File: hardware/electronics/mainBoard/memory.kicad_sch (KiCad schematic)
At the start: 16 parts, among them J2 MEM2067-02-180-00-A, U3 W25Q128JVP, U4 M24512-DRE

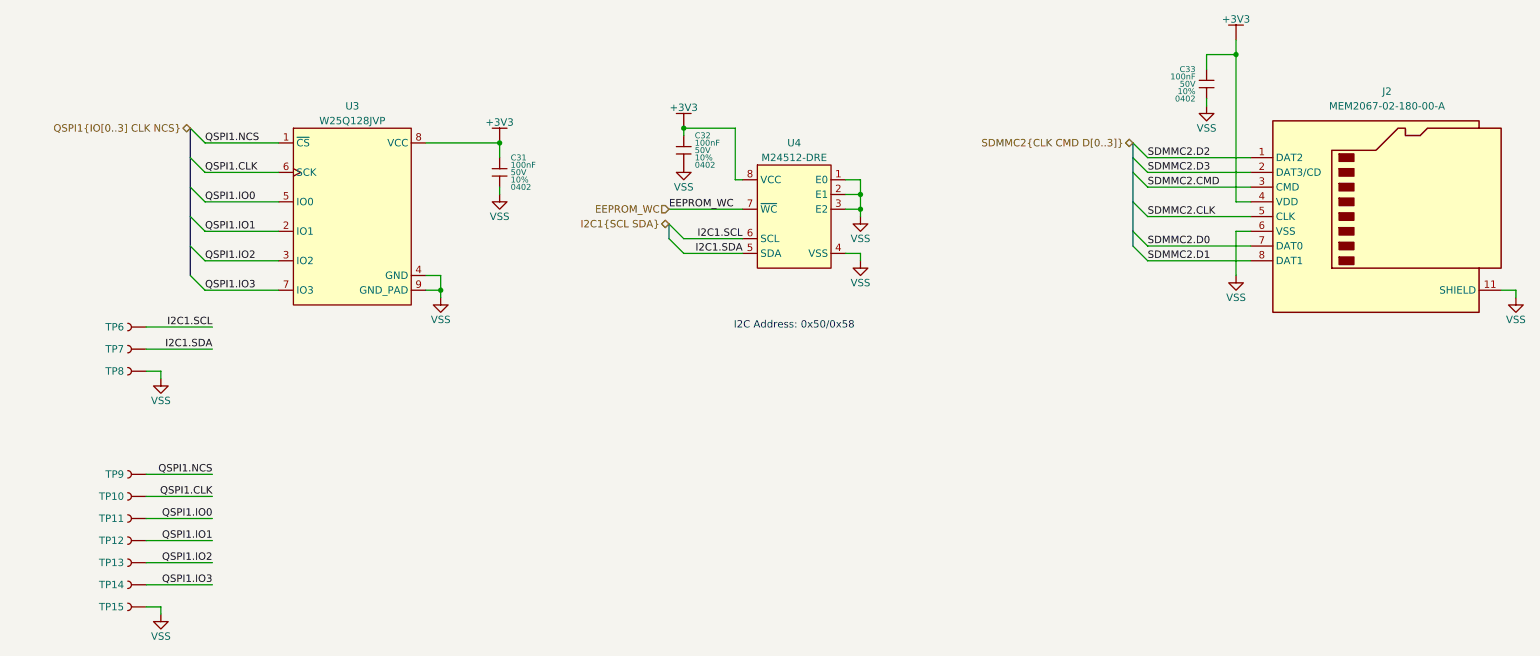
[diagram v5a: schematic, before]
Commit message: updated symbol refs
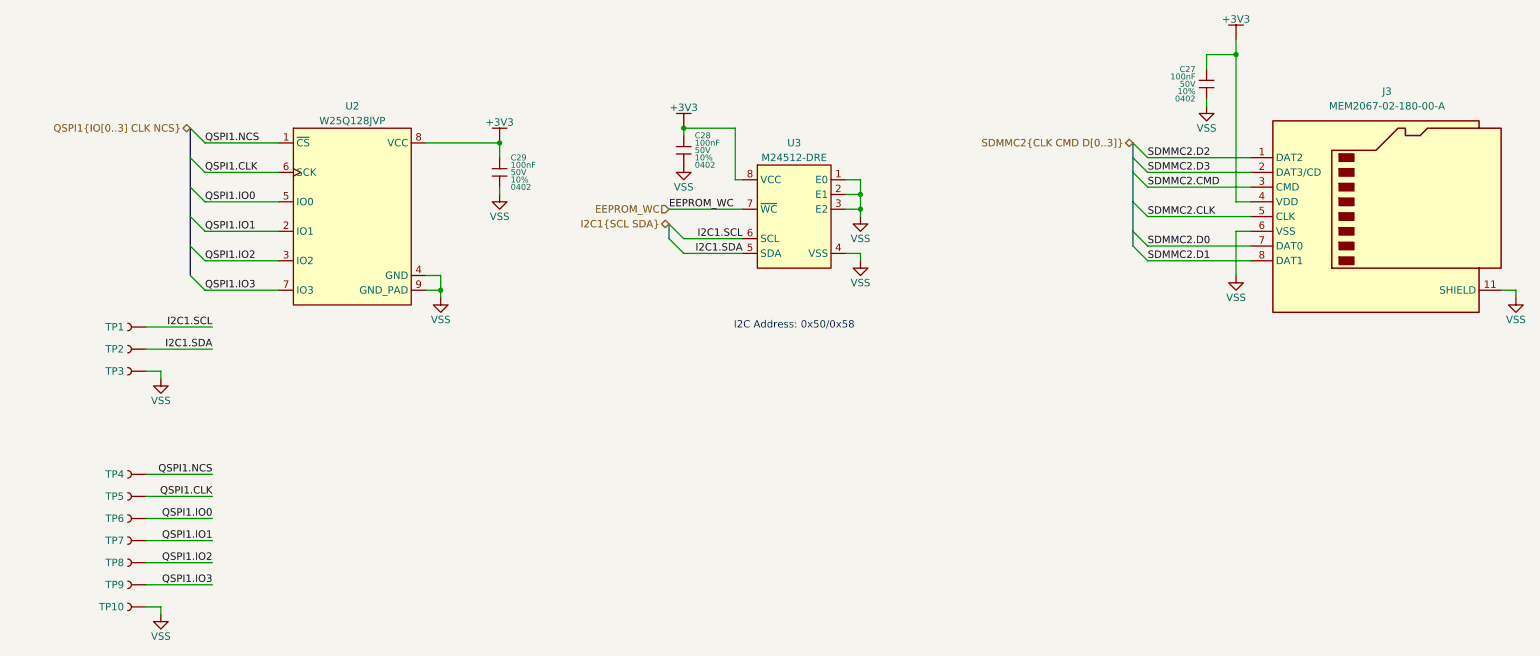
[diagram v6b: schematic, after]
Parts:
- renumbered C33 to C27, C32 to C28, C31 to C29, J2 to J3, TP6 to TP1, TP15 to TP10, TP7 to TP2, TP8 to TP3, TP9 to TP4, TP10 to TP5, TP11 to TP6, TP12 to TP7, TP13 to TP8, TP14 to TP9, U3 to U2, U4 to U3
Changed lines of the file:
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@@
 		(dnp no)
 		(fields_autoplaced yes)
-		(property "Reference" "#PWR068"
+		(property "Reference" "#PWR065"
 			(at 88.9 95.25 0)
 			(effects
@@
 			(project ""
 				(path "/be16e32f-2ccf-4272-9ec7-94d5fe7a55e0/bf9ac865-aa9a-42a1-8ada-6ec99a5fbf41"
-					(reference "#PWR068")
+					(reference "#PWR065")
 					(unit 1)
 				)
@@
 		(dnp no)
 		(fields_autoplaced yes)
-		(property "Reference" "#PWR070"
+		(property "Reference" "#PWR064"
 			(at 120.65 92.71 0)
 			(effects
@@
 			(project "mainBoard"
 				(path "/be16e32f-2ccf-4272-9ec7-94d5fe7a55e0/bf9ac865-aa9a-42a1-8ada-6ec99a5fbf41"
-					(reference "#PWR070")
+					(reference "#PWR064")
 					(unit 1)
 				)
@@
 		(dnp no)
 		(fields_autoplaced yes)
-		(property "Reference" "J2"
+		(property "Reference" "J3"
 			(at 241.935 86.36 0)
 			(effects
@@
 			(project ""
 				(path "/be16e32f-2ccf-4272-9ec7-94d5fe7a55e0/bf9ac865-aa9a-42a1-8ada-6ec99a5fbf41"
-					(reference "J2")
+					(reference "J3")
 					(unit 1)
 				)
@@
 		(on_board yes)
 		(dnp no)
-		(property "Reference" "C33"
+		(property "Reference" "C27"
 			(at 208.915 82.55 0)
 			(do_not_autoplace yes)
@@
 			(project "mainBoard"
 				(path "/be16e32f-2ccf-4272-9ec7-94d5fe7a55e0/bf9ac865-aa9a-42a1-8ada-6ec99a5fbf41"
-					(reference "C33")
+					(reference "C27")
 					(unit 1)
 				)
@@
 		(dnp no)
 		(fields_autoplaced yes)
-		(property "Reference" "TP15"
+		(property "Reference" "TP10"
 			(at 24.13 175.26 0)
 			(do_not_autoplace yes)
@@
 			(project "mainBoard"
 				(path "/be16e32f-2ccf-4272-9ec7-94d5fe7a55e0/bf9ac865-aa9a-42a1-8ada-6ec99a5fbf41"
-					(reference "TP15")
+					(reference "TP10")
 					(unit 1)
 				)
@@
 		(dnp no)
 		(fields_autoplaced yes)
-		(property "Reference" "#PWR077"
+		(property "Reference" "#PWR072"
 			(at 264.16 121.92 0)
 			(effects
@@
 			(project "mainBoard"
 				(path "/be16e32f-2ccf-4272-9ec7-94d5fe7a55e0/bf9ac865-aa9a-42a1-8ada-6ec99a5fbf41"
-					(reference "#PWR077")
+					(reference "#PWR072")
 					(unit 1)
 				)
@@
 		(dnp no)
 		(fields_autoplaced yes)
-		(property "Reference" "TP8"
+		(property "Reference" "TP3"
 			(at 24.13 134.62 0)
 			(do_not_autoplace yes)
@@
 			(project "mainBoard"
 				(path "/be16e32f-2ccf-4272-9ec7-94d5fe7a55e0/bf9ac865-aa9a-42a1-8ada-6ec99a5fbf41"
-					(reference "TP8")
+					(reference "TP3")
 					(unit 1)
 				)
@@
 		(dnp no)
 		(fields_autoplaced yes)
-		(property "Reference" "TP7"
+		(property "Reference" "TP2"
 			(at 24.13 130.81 0)
 			(do_not_autoplace yes)
@@
 			(project "mainBoard"
 				(path "/be16e32f-2ccf-4272-9ec7-94d5fe7a55e0/bf9ac865-aa9a-42a1-8ada-6ec99a5fbf41"
-					(reference "TP7")
+					(reference "TP2")
 					(unit 1)
 				)
@@
 		(dnp no)
 		(fields_autoplaced yes)
-		(property "Reference" "#PWR076"
+		(property "Reference" "#PWR070"
 			(at 215.9 118.11 0)
 			(effects
@@
 			(project "mainBoard"
 				(path "/be16e32f-2ccf-4272-9ec7-94d5fe7a55e0/bf9ac865-aa9a-42a1-8ada-6ec99a5fbf41"
-					(reference "#PWR076")
+					(reference "#PWR070")
 					(unit 1)
 				)
@@
 		(dnp no)
 		(fields_autoplaced yes)
-		(property "Reference" "C32"
+		(property "Reference" "C28"
 			(at 122.555 93.98 0)
 			(do_not_autoplace yes)
@@
 			(project "mainBoard"
 				(path "/be16e32f-2ccf-4272-9ec7-94d5fe7a55e0/bf9ac865-aa9a-42a1-8ada-6ec99a5fbf41"
-					(reference "C32")
+					(reference "C28")
 					(unit 1)
 				)
@@
 		(dnp no)
 		(fields_autoplaced yes)
-		(property "Reference" "TP14"
+		(property "Reference" "TP9"
 			(at 24.13 171.45 0)
 			(do_not_autoplace yes)
@@
 			(project "mainBoard"
 				(path "/be16e32f-2ccf-4272-9ec7-94d5fe7a55e0/bf9ac865-aa9a-42a1-8ada-6ec99a5fbf41"
-					(reference "TP14")
+					(reference "TP9")
 					(unit 1)
 				)
@@
 		(dnp no)
 		(fields_autoplaced yes)
-		(property "Reference" "C31"
+		(property "Reference" "C29"
 			(at 90.805 97.79 0)
 			(do_not_autoplace yes)
@@
 			(project "mainBoard"
 				(path "/be16e32f-2ccf-4272-9ec7-94d5fe7a55e0/bf9ac865-aa9a-42a1-8ada-6ec99a5fbf41"
-					(reference "C31")
+					(reference "C29")
 					(unit 1)
 				)
@@
 		(dnp no)
 		(fields_autoplaced yes)
-		(property "Reference" "TP12"
+		(property "Reference" "TP7"
 			(at 24.13 163.83 0)
 			(do_not_autoplace yes)
@@
 			(project "mainBoard"
 				(path "/be16e32f-2ccf-4272-9ec7-94d5fe7a55e0/bf9ac865-aa9a-42a1-8ada-6ec99a5fbf41"
-					(reference "TP12")
+					(reference "TP7")
 					(unit 1)
 				)
@@
 		(dnp no)
 		(fields_autoplaced yes)
-		(property "Reference" "U3"
+		(property "Reference" "U2"
 			(at 63.5 88.9 0)
 			(do_not_autoplace yes)
@@
 			(project ""
 				(path "/be16e32f-2ccf-4272-9ec7-94d5fe7a55e0/bf9ac865-aa9a-42a1-8ada-6ec99a5fbf41"
-					(reference "U3")
+					(reference "U2")
 					(unit 1)
 				)
@@
 		(dnp no)
 		(fields_autoplaced yes)
-		(property "Reference" "#PWR069"
+		(property "Reference" "#PWR067"
 			(at 88.9 104.14 0)
 			(effects
@@
 			(project "mainBoard"
 				(path "/be16e32f-2ccf-4272-9ec7-94d5fe7a55e0/bf9ac865-aa9a-42a1-8ada-6ec99a5fbf41"
-					(reference "#PWR069")
+					(reference "#PWR067")
 					(unit 1)
 				)
@@
 		(dnp no)
 		(fields_autoplaced yes)
-		(property "Reference" "TP13"
+		(property "Reference" "TP8"
 			(at 24.13 167.64 0)
 			(do_not_autoplace yes)
@@
 			(project "mainBoard"
 				(path "/be16e32f-2ccf-4272-9ec7-94d5fe7a55e0/bf9ac865-aa9a-42a1-8ada-6ec99a5fbf41"
-					(reference "TP13")
+					(reference "TP8")
 					(unit 1)
 				)
@@
 		(dnp no)
 		(fields_autoplaced yes)
-		(property "Reference" "#PWR066"
+		(property "Reference" "#PWR074"
 			(at 30.48 176.53 0)
 			(effects
@@
 			(project "mainBoard"
 				(path "/be16e32f-2ccf-4272-9ec7-94d5fe7a55e0/bf9ac865-aa9a-42a1-8ada-6ec99a5fbf41"
-					(reference "#PWR066")
+					(reference "#PWR074")
 					(unit 1)
 				)
@@
 		(dnp no)
 		(fields_autoplaced yes)
-		(property "Reference" "TP9"
+		(property "Reference" "TP4"
 			(at 24.13 152.4 0)
 			(do_not_autoplace yes)
@@
 			(project "mainBoard"
 				(path "/be16e32f-2ccf-4272-9ec7-94d5fe7a55e0/bf9ac865-aa9a-42a1-8ada-6ec99a5fbf41"
-					(reference "TP9")
+					(reference "TP4")
 					(unit 1)
 				)
@@
 		(dnp no)
 		(fields_autoplaced yes)
-		(property "Reference" "U4"
+		(property "Reference" "U3"
 			(at 139.7 95.25 0)
 			(do_not_autoplace yes)
@@
 			(project ""
 				(path "/be16e32f-2ccf-4272-9ec7-94d5fe7a55e0/bf9ac865-aa9a-42a1-8ada-6ec99a5fbf41"
-					(reference "U4")
+					(reference "U3")
 					(unit 1)
 				)
@@
 		(dnp no)
 		(fields_autoplaced yes)
-		(property "Reference" "#PWR073"
+		(property "Reference" "#PWR069"
 			(at 151.13 115.57 0)
 			(effects
@@
 			(project "mainBoard"
 				(path "/be16e32f-2ccf-4272-9ec7-94d5fe7a55e0/bf9ac865-aa9a-42a1-8ada-6ec99a5fbf41"
-					(reference "#PWR073")
+					(reference "#PWR069")
 					(unit 1)
 				)
@@
 		(dnp no)
 		(fields_autoplaced yes)
-		(property "Reference" "#PWR074"
+		(property "Reference" "#PWR063"
 			(at 210.82 88.9 0)
 			(effects
@@
 			(project "mainBoard"
 				(path "/be16e32f-2ccf-4272-9ec7-94d5fe7a55e0/bf9ac865-aa9a-42a1-8ada-6ec99a5fbf41"
-					(reference "#PWR074")
+					(reference "#PWR063")
 					(unit 1)
 				)
@@
 		(dnp no)
 		(fields_autoplaced yes)
-		(property "Reference" "#PWR075"
+		(property "Reference" "#PWR062"
 			(at 215.9 77.47 0)
 			(effects
@@
 			(project "mainBoard"
 				(path "/be16e32f-2ccf-4272-9ec7-94d5fe7a55e0/bf9ac865-aa9a-42a1-8ada-6ec99a5fbf41"
-					(reference "#PWR075")
+					(reference "#PWR062")
 					(unit 1)
 				)
@@
 		(dnp no)
 		(fields_autoplaced yes)
-		(property "Reference" "TP10"
+		(property "Reference" "TP5"
 			(at 24.13 156.21 0)
 			(do_not_autoplace yes)
@@
 			(project "mainBoard"
 				(path "/be16e32f-2ccf-4272-9ec7-94d5fe7a55e0/bf9ac865-aa9a-42a1-8ada-6ec99a5fbf41"
-					(reference "TP10")
+					(reference "TP5")
 					(unit 1)
 				)
@@
 		(dnp no)
 		(fields_autoplaced yes)
-		(property "Reference" "TP6"
+		(property "Reference" "TP1"
 			(at 24.13 127 0)
 			(do_not_autoplace yes)
@@
 			(project "mainBoard"
 				(path "/be16e32f-2ccf-4272-9ec7-94d5fe7a55e0/bf9ac865-aa9a-42a1-8ada-6ec99a5fbf41"
-					(reference "TP6")
+					(reference "TP1")
 					(unit 1)
 				)
@@
 		(dnp no)
 		(fields_autoplaced yes)
-		(property "Reference" "#PWR065"
+		(property "Reference" "#PWR073"
 			(at 30.48 135.89 0)
 			(effects
@@
 			(project "mainBoard"
 				(path "/be16e32f-2ccf-4272-9ec7-94d5fe7a55e0/bf9ac865-aa9a-42a1-8ada-6ec99a5fbf41"
-					(reference "#PWR065")
+					(reference "#PWR073")
 					(unit 1)
 				)
@@
 		(dnp no)
 		(fields_autoplaced yes)
-		(property "Reference" "#PWR067"
+		(property "Reference" "#PWR071"
 			(at 78.74 121.92 0)
 			(effects
@@
 			(project ""
 				(path "/be16e32f-2ccf-4272-9ec7-94d5fe7a55e0/bf9ac865-aa9a-42a1-8ada-6ec99a5fbf41"
-					(reference "#PWR067")
+					(reference "#PWR071")
 					(unit 1)
 				)
@@
 		(dnp no)
 		(fields_autoplaced yes)
-		(property "Reference" "TP11"
+		(property "Reference" "TP6"
 			(at 24.13 160.02 0)
 			(do_not_autoplace yes)
@@
 			(project "mainBoard"
 				(path "/be16e32f-2ccf-4272-9ec7-94d5fe7a55e0/bf9ac865-aa9a-42a1-8ada-6ec99a5fbf41"
-					(reference "TP11")
+					(reference "TP6")
 					(unit 1)
 				)
@@
 		(dnp no)
 		(fields_autoplaced yes)
-		(property "Reference" "#PWR072"
+		(property "Reference" "#PWR068"
 			(at 151.13 107.95 0)
 			(effects
@@
 			(project "mainBoard"
 				(path "/be16e32f-2ccf-4272-9ec7-94d5fe7a55e0/bf9ac865-aa9a-42a1-8ada-6ec99a5fbf41"
-					(reference "#PWR072")
+					(reference "#PWR068")
 					(unit 1)
 				)
@@
 		(dnp no)
 		(fields_autoplaced yes)
-		(property "Reference" "#PWR071"
+		(property "Reference" "#PWR066"
 			(at 120.65 99.06 0)
 			(effects
@@
 			(project "mainBoard"
 				(path "/be16e32f-2ccf-4272-9ec7-94d5fe7a55e0/bf9ac865-aa9a-42a1-8ada-6ec99a5fbf41"
-					(reference "#PWR071")
-					(unit 1)
-				)
+					(reference "#PWR066")
+					(unit 1)
+				)

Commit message: assigned FPs
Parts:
- J3: footprint (none) -> lib_connectors:MEM2067-02-180-00-A
- U2: footprint (none) -> lib_ICs:WFDFN8P127_600X500X75L60X40N
- U3: footprint (none) -> lib_ICs:SOIC127P600x175-8
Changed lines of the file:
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@@
 			)
 		)
-		(property "Footprint" ""
+		(property "Footprint" "lib_connectors:MEM2067-02-180-00-A"
 			(at 293.37 90.17 0)
 			(effects
@@
 			)
 		)
-		(property "Footprint" ""
+		(property "Footprint" "lib_ICs:WFDFN8P127_600X500X75L60X40N"
 			(at 63.5 107.95 0)
 			(effects
@@
 			)
 		)
-		(property "Footprint" ""
+		(property "Footprint" "lib_ICs:SOIC127P600x175-8"
 			(at 139.7 107.95 0)
 			(effects

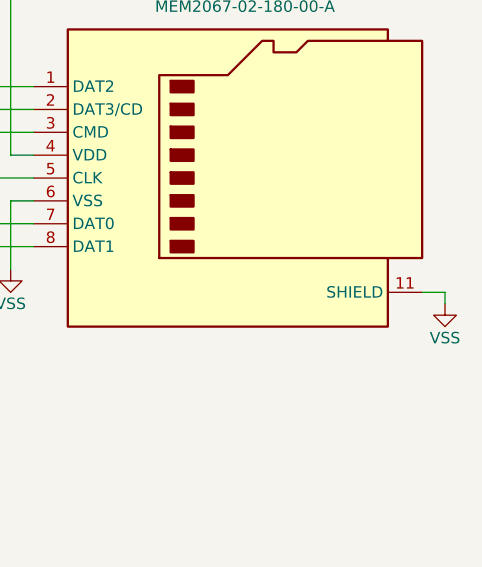
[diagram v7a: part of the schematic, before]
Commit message: added footprints to symbols
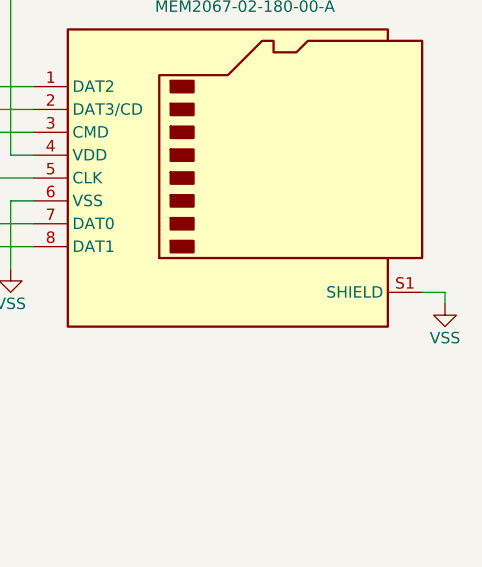
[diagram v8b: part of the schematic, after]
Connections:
- net VSS: now also J3.S1 (SHIELD), J3.S2 (SHIELD), J3.S3 (SHIELD), J3.S4 (SHIELD); no longer J3.11 (SHIELD)
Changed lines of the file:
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@@
 			)
 		)
-		(pin "11"
+		(pin "S1"
 		)
 		(pin "4"
@@
 		(pin "2"
 		)
+		(pin "S2"
+		)
+		(pin "S3"
+		)
+		(pin "S4"
+		)
 		(instances
